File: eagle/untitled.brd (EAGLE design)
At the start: 50 x 50 mm, 38 parts, among them J1 JTAG, U1 MMA3202KEG

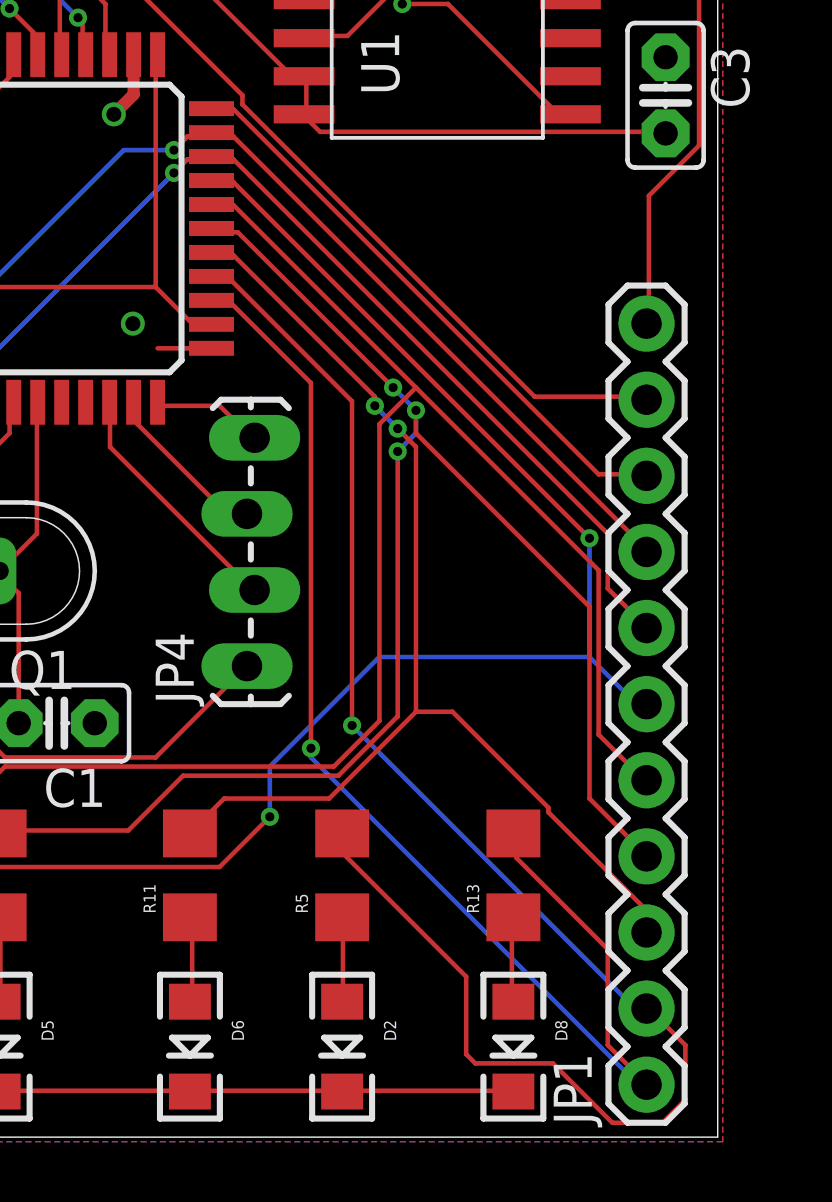
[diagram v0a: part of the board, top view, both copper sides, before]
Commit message: Add pin labels.
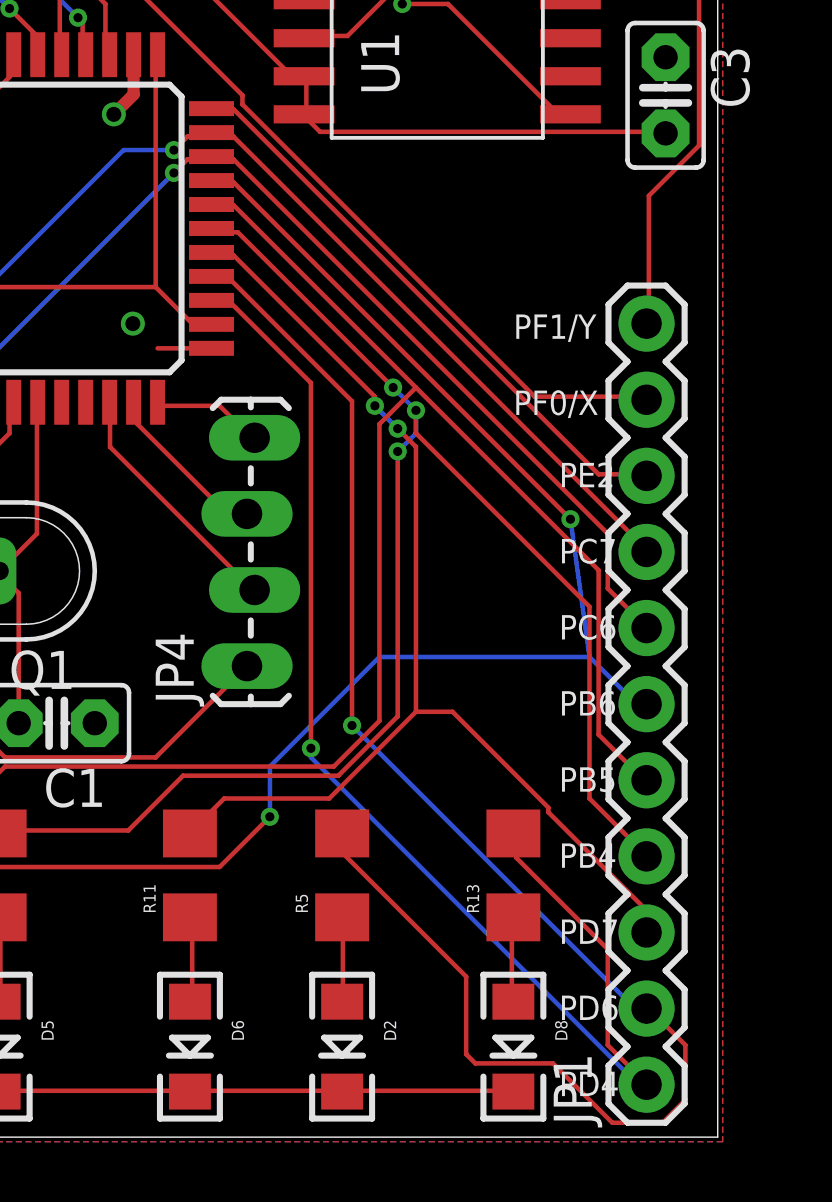
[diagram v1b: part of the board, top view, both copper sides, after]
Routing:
- net PD4: track 42.9 -> 44.1 mm
- net PD6: track 52.3 -> 53.4 mm
- net PB5: track 57.3 -> 57.9 mm
- net PE2: track 19.6 -> 20.2 mm
- net PD7: track 39.0 -> 39.7 mm
- net Y: track 37.3 -> 37.9 mm
- net PC6: track 56.3 -> 56.9 mm
- net PB4: track 52.8 -> 53.4 mm
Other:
- board text added: "PB4"
- board text added: "PB5"
- board text added: "PB6"
- board text added: "PC6"
- board text added: "PC7"
- board text added: "PD4"
- board text added: "PD6"
- board text added: "PD7"
- board text added: "PE2"
- board text added: "PF0/X"
- board text added: "PF1/Y"
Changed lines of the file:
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@@
 <wire x1="0" y1="80" x2="0" y2="30" width="0" layer="20"/>
 <text x="41.91" y="77.47" size="1.778" layer="21">UP -&gt;</text>
+<text x="44.704" y="31.369" size="0.8128" layer="21" font="vector">PD4</text>
+<text x="44.704" y="33.909" size="0.8128" layer="21" font="vector">PD6</text>
+<text x="44.704" y="36.449" size="0.8128" layer="21" font="vector">PD7</text>
+<text x="44.704" y="38.989" size="0.8128" layer="21" font="vector">PB4</text>
+<text x="44.704" y="41.529" size="0.8128" layer="21" font="vector">PB5</text>
+<text x="44.704" y="44.069" size="0.8128" layer="21" font="vector">PB6</text>
+<text x="44.704" y="46.609" size="0.8128" layer="21" font="vector">PC6</text>
+<text x="44.704" y="49.149" size="0.8128" layer="21" font="vector">PC7</text>
+<text x="44.704" y="51.689" size="0.8128" layer="21" font="vector">PE2</text>
+<text x="43.18" y="54.102" size="0.8128" layer="21" font="vector">PF0/X</text>
+<text x="43.18" y="56.642" size="0.8128" layer="21" font="vector">PF1/Y</text>
 </plain>
 <attributes>
@@
 <wire x1="34.1376" y1="64.77" x2="34.1376" y2="64.4652" width="0.1524" layer="1"/>
 <wire x1="28.194" y1="70.7136" x2="34.1376" y2="64.77" width="0.1524" layer="1"/>
-<wire x1="47.5488" y1="54.7116" x2="47.625" y2="54.61" width="0.1524" layer="1"/>
+<wire x1="47.5488" y1="54.7116" x2="48.26" y2="54.61" width="0.1524" layer="1"/>
 <wire x1="28.194" y1="70.7136" x2="28.575" y2="71.12" width="0.1524" layer="1"/>
 </signal>
@@
 <wire x1="49.3776" y1="75.1332" x2="49.3776" y2="63.0936" width="0.1524" layer="1"/>
 <wire x1="48.3108" y1="76.2" x2="49.3776" y2="75.1332" width="0.1524" layer="1"/>
-<wire x1="47.7012" y1="57.15" x2="47.625" y2="57.15" width="0.1524" layer="1"/>
+<wire x1="47.7012" y1="57.15" x2="48.26" y2="57.15" width="0.1524" layer="1"/>
 <wire x1="48.3108" y1="76.2" x2="48.26" y2="76.2" width="0.1524" layer="1"/>
 <wire x1="26.3652" y1="65.3796" x2="26.3652" y2="65.9892" width="0.1524" layer="1"/>
@@
 <wire x1="41.148" y1="44.196" x2="44.3484" y2="40.9956" width="0.1524" layer="1"/>
 <wire x1="39.9288" y1="44.196" x2="41.148" y2="44.196" width="0.1524" layer="1"/>
-<wire x1="47.5488" y1="36.8808" x2="47.625" y2="36.83" width="0.1524" layer="1"/>
+<wire x1="47.5488" y1="36.8808" x2="48.26" y2="36.83" width="0.1524" layer="1"/>
 <via x="38.5572" y="54.4068" extent="1-16" drill="0.3048"/>
 <via x="39.3192" y="53.6448" extent="1-16" drill="0.3048"/>
@@
 <wire x1="47.5488" y1="31.8516" x2="47.244" y2="31.8516" width="0.1524" layer="16"/>
 <wire x1="33.2232" y1="57.912" x2="33.105" y2="57.925" width="0.1524" layer="1"/>
-<wire x1="47.5488" y1="31.8516" x2="47.625" y2="31.75" width="0.1524" layer="16"/>
+<wire x1="47.5488" y1="31.8516" x2="48.26" y2="31.75" width="0.1524" layer="16"/>
 <via x="36.4236" y="42.9768" extent="1-16" drill="0.3048"/>
 <wire x1="43.2816" y1="39.3192" x2="43.2816" y2="40.0812" width="0.1524" layer="1"/>
@@
 <wire x1="47.5488" y1="31.8516" x2="46.3296" y2="33.0708" width="0.1524" layer="1"/>
 <wire x1="43.2816" y1="40.0812" x2="43.18" y2="40.135" width="0.1524" layer="1"/>
-<wire x1="47.5488" y1="31.8516" x2="47.625" y2="31.75" width="0.1524" layer="1"/>
+<wire x1="47.5488" y1="31.8516" x2="48.26" y2="31.75" width="0.1524" layer="1"/>
 </signal>
 <signal name="PD6">
@@
 <wire x1="37.7952" y1="43.7388" x2="37.7952" y2="54.5592" width="0.1524" layer="1"/>
 <wire x1="47.244" y1="34.29" x2="37.7952" y2="43.7388" width="0.1524" layer="16"/>
-<wire x1="47.625" y1="34.29" x2="47.244" y2="34.29" width="0.1524" layer="16"/>
+<wire x1="48.26" y1="34.29" x2="47.244" y2="34.29" width="0.1524" layer="16"/>
 <wire x1="33.2232" y1="58.674" x2="33.105" y2="58.725" width="0.1524" layer="1"/>
 <wire x1="37.4904" y1="39.4716" x2="37.4904" y2="40.0812" width="0.1524" layer="1"/>
@@
 <wire x1="47.7012" y1="34.29" x2="48.9204" y2="33.0708" width="0.1524" layer="1"/>
 <wire x1="37.4904" y1="40.0812" x2="37.465" y2="40.135" width="0.1524" layer="1"/>
-<wire x1="47.7012" y1="34.29" x2="47.625" y2="34.29" width="0.1524" layer="1"/>
+<wire x1="47.7012" y1="34.29" x2="48.26" y2="34.29" width="0.1524" layer="1"/>
 <via x="37.7952" y="43.7388" extent="1-16" drill="0.3048"/>
 </signal>
@@
 <contactref element="R6" pad="2"/>
 <wire x1="33.8328" y1="61.8744" x2="33.2232" y2="61.8744" width="0.1524" layer="1"/>
-<wire x1="45.72" y1="49.9872" x2="33.8328" y2="61.8744" width="0.1524" layer="1"/>
-<wire x1="45.72" y1="46.0248" x2="45.72" y2="49.9872" width="0.1524" layer="16"/>
+<wire x1="45.085" y1="50.6222" x2="33.8328" y2="61.8744" width="0.1524" layer="1"/>
+<wire x1="45.72" y1="46.0248" x2="45.085" y2="50.6222" width="0.1524" layer="16"/>
 <wire x1="47.244" y1="44.5008" x2="45.72" y2="46.0248" width="0.1524" layer="16"/>
 <wire x1="47.5488" y1="44.5008" x2="47.244" y2="44.5008" width="0.1524" layer="16"/>
 <wire x1="33.2232" y1="61.8744" x2="33.105" y2="61.925" width="0.1524" layer="1"/>
-<wire x1="47.5488" y1="44.5008" x2="47.625" y2="44.45" width="0.1524" layer="16"/>
+<wire x1="47.5488" y1="44.5008" x2="48.26" y2="44.45" width="0.1524" layer="16"/>
 <wire x1="14.6304" y1="42.2148" x2="14.6304" y2="40.2336" width="0.1524" layer="1"/>
 <wire x1="17.3736" y1="44.958" x2="14.6304" y2="42.2148" width="0.1524" layer="1"/>
@@
 <wire x1="45.72" y1="46.0248" x2="38.7096" y2="46.0248" width="0.1524" layer="16"/>
 <wire x1="14.6304" y1="40.2336" x2="14.605" y2="40.135" width="0.1524" layer="1"/>
-<via x="45.72" y="49.9872" extent="1-16" drill="0.3048"/>
+<via x="45.085" y="50.6222" extent="1-16" drill="0.3048"/>
 <via x="35.052" y="40.6908" extent="1-16" drill="0.3048"/>
 </signal>
@@
 <wire x1="47.5488" y1="47.0916" x2="46.3296" y2="48.3108" width="0.1524" layer="1"/>
 <wire x1="33.2232" y1="62.6364" x2="33.105" y2="62.725" width="0.1524" layer="1"/>
-<wire x1="47.5488" y1="47.0916" x2="47.625" y2="46.99" width="0.1524" layer="1"/>
+<wire x1="47.5488" y1="47.0916" x2="48.26" y2="46.99" width="0.1524" layer="1"/>
 <wire x1="9.906" y1="40.2336" x2="8.382" y2="40.2336" width="0.1524" layer="1"/>
 <wire x1="20.2692" y1="50.5968" x2="9.906" y2="40.2336" width="0.1524" layer="1"/>
@@
 <wire x1="47.7012" y1="49.53" x2="33.8328" y2="63.3984" width="0.1524" layer="1"/>
 <wire x1="33.2232" y1="63.3984" x2="33.105" y2="63.525" width="0.1524" layer="1"/>
-<wire x1="47.7012" y1="49.53" x2="47.625" y2="49.53" width="0.1524" layer="1"/>
+<wire x1="47.7012" y1="49.53" x2="48.26" y2="49.53" width="0.1524" layer="1"/>
 <wire x1="6.2484" y1="40.2336" x2="1.9812" y2="40.2336" width="0.1524" layer="1"/>
 <wire x1="17.526" y1="51.5112" x2="6.2484" y2="40.2336" width="0.1524" layer="1"/>
@@
 <wire x1="47.5488" y1="39.4716" x2="45.72" y2="41.3004" width="0.1524" layer="1"/>
 <wire x1="33.2232" y1="60.198" x2="33.105" y2="60.325" width="0.1524" layer="1"/>
-<wire x1="47.5488" y1="39.4716" x2="47.625" y2="39.37" width="0.1524" layer="1"/>
+<wire x1="47.5488" y1="39.4716" x2="48.26" y2="39.37" width="0.1524" layer="1"/>
 <wire x1="30.3276" y1="40.2336" x2="26.0604" y2="40.2336" width="0.1524" layer="1"/>
 <wire x1="32.1564" y1="42.0624" x2="30.3276" y2="40.2336" width="0.1524" layer="1"/>
@@
 <wire x1="47.5488" y1="41.91" x2="46.0248" y2="43.434" width="0.1524" layer="1"/>
 <wire x1="33.2232" y1="61.1124" x2="33.105" y2="61.125" width="0.1524" layer="1"/>
-<wire x1="47.5488" y1="41.91" x2="47.625" y2="41.91" width="0.1524" layer="1"/>
+<wire x1="47.5488" y1="41.91" x2="48.26" y2="41.91" width="0.1524" layer="1"/>
 <wire x1="24.0792" y1="40.2336" x2="20.4216" y2="40.2336" width="0.1524" layer="1"/>
 <wire x1="26.2128" y1="42.3672" x2="24.0792" y2="40.2336" width="0.1524" layer="1"/>
@@
 <wire x1="47.5488" y1="52.1208" x2="46.0248" y2="52.1208" width="0.1524" layer="1"/>
 <wire x1="33.2232" y1="64.3128" x2="33.105" y2="64.325" width="0.1524" layer="1"/>
-<wire x1="47.5488" y1="52.1208" x2="47.625" y2="52.07" width="0.1524" layer="1"/>
+<wire x1="47.5488" y1="52.1208" x2="48.26" y2="52.07" width="0.1524" layer="1"/>
 </signal>
 <signal name="N$2">

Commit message: Smash and rework some labels.
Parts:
- moved JP1 0.63 mm to (48.3, 31.8)
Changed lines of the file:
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@@
 </element>
 <element name="R3" library="SparkFun-Passives" package="1206" value="10k" x="19.685" y="52.705"/>
-<element name="Q1" library="special" package="QS" value="" x="23.495" y="48.895" rot="R180"/>
-<element name="C1" library="capacitor-wima" package="C2.5-2" value="" x="27.94" y="43.815" rot="R180"/>
+<element name="Q1" library="special" package="QS" value="" x="23.495" y="48.895" smashed="yes" rot="R180">
+<attribute name="VALUE" x="28.575" y="52.832" size="1.27" layer="27" ratio="10" rot="R180"/>
+<attribute name="NAME" x="31.75" y="50.673" size="1.27" layer="25" ratio="10" rot="R180"/>
+</element>
+<element name="C1" library="capacitor-wima" package="C2.5-2" value="" x="27.94" y="43.815" smashed="yes" rot="R180">
+<attribute name="NAME" x="29.591" y="46.736" size="1.27" layer="25" ratio="10" rot="R180"/>
+<attribute name="VALUE" x="29.591" y="46.609" size="1.27" layer="27" ratio="10" rot="R180"/>
+</element>
 <element name="C2" library="capacitor-wima" package="C2.5-2" value="" x="19.05" y="43.815"/>
 <element name="U1" library="gipi" package="SOIC20" value="MMA3202KEG" x="40.64" y="69.85"/>
-<element name="G1" library="battery" package="10MM_SM_COIN_CELL_CLIP" value="BAT" x="5.715" y="50.165" rot="R90"/>
-<element name="C3" library="capacitor-wima" package="C2.5-2" value="" x="48.26" y="64.77" rot="R270"/>
+<element name="G1" library="battery" package="10MM_SM_COIN_CELL_CLIP" value="BAT" x="5.715" y="50.165" smashed="yes" rot="R90">
+<attribute name="NAME" x="2.99248125" y="56.20125" size="1.27" layer="25" font="vector" rot="R90"/>
+<attribute name="VALUE" x="12.15435" y="45.68245" size="1.27" layer="27" font="vector" rot="R90"/>
+</element>
+<element name="C3" library="capacitor-wima" package="C2.5-2" value="" x="48.26" y="64.77" smashed="yes" rot="R270">
+<attribute name="NAME" x="47.244" y="67.691" size="1.27" layer="25" ratio="10"/>
+<attribute name="VALUE" x="45.466" y="66.421" size="1.27" layer="27" ratio="10" rot="R270"/>
+</element>
 <element name="SJ1" library="SparkFun-Retired" package="SJ_3_PASTE2&amp;3" value="" x="29.21" y="77.47" rot="R180"/>
 <element name="R9" library="SparkFun-Passives" package="1206" value="10k" x="33.02" y="76.2" rot="R270"/>
 <element name="R10" library="SparkFun-Passives" package="1206" value="10k" x="24.13" y="71.12" rot="R180"/>
 <element name="C4" library="capacitor-wima" package="C2.5-2" value="" x="29.845" y="71.12" rot="R180"/>
-<element name="C5" library="capacitor-wima" package="C2.5-2" value="" x="48.26" y="74.93" rot="R90"/>
+<element name="C5" library="capacitor-wima" package="C2.5-2" value="" x="48.26" y="74.93" smashed="yes" rot="R90">
+<attribute name="NAME" x="49.276" y="72.136" size="1.27" layer="25" ratio="10" rot="R180"/>
+<attribute name="VALUE" x="51.054" y="73.279" size="1.27" layer="27" ratio="10" rot="R90"/>
+</element>
 <element name="C6" library="capacitor-wima" package="C2.5-2" value="1uf" x="14.605" y="64.77" rot="R180"/>
 <element name="JP4" library="SparkFun-Connectors" package="1X04_LOCK_LONGPADS" value="SERIAL" x="34.29" y="45.72" rot="R90"/>
 <element name="JP5" library="SparkFun-Connectors" package="2X3" value="PRG" x="13.335" y="60.325" rot="R270"/>
-<element name="JP1" library="SparkFun-Connectors" package="1X11" value="M11PTH" x="47.625" y="31.75" rot="R90"/>
+<element name="JP1" library="SparkFun-Connectors" package="1X11" value="M11PTH" x="48.26" y="31.75" smashed="yes" rot="R90">
+<attribute name="NAME" x="48.9712" y="26.5938" size="1.27" layer="25" ratio="10" rot="R90"/>
+<attribute name="VALUE" x="51.435" y="30.48" size="1.27" layer="27" rot="R90"/>
+</element>
 <element name="R4" library="SparkFun-Passives" package="1206" value="" x="1.905" y="38.735" rot="R90"/>
 <element name="D1" library="SparkFun-LED" package="LED-1206" value="" x="1.905" y="33.02" rot="R270"/>
@@
 <element name="R12" library="SparkFun-Passives" package="1206" value="" x="8.255" y="38.735" rot="R90"/>
 <element name="R13" library="SparkFun-Passives" package="1206" value="" x="43.18" y="38.735" rot="R90"/>
-<element name="J1" library="con-headers-jp" package="DIL-2MM-2X05" value="JTAG" x="22.225" y="76.835"/>
+<element name="J1" library="con-headers-jp" package="DIL-2MM-2X05" value="JTAG" x="22.225" y="76.835" smashed="yes">
+<attribute name="NAME" x="16.225" y="76.105" size="1.016" layer="25" ratio="18" rot="R90"/>
+<attribute name="VALUE" x="18.51" y="73.675" size="0.8128" layer="27" ratio="10" rot="R180"/>
+</element>
 </elements>
 <signals>

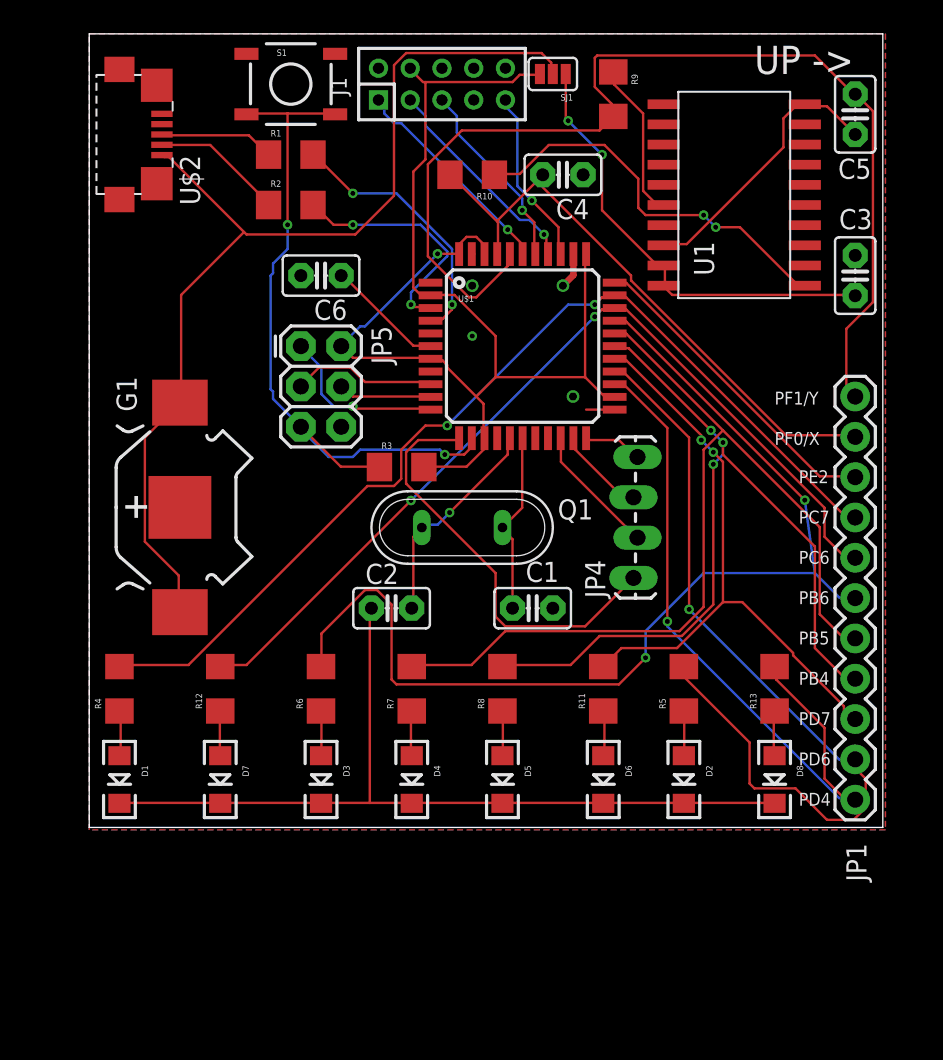
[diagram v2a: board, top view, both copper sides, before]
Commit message: Replace usb micro connector with mini type.
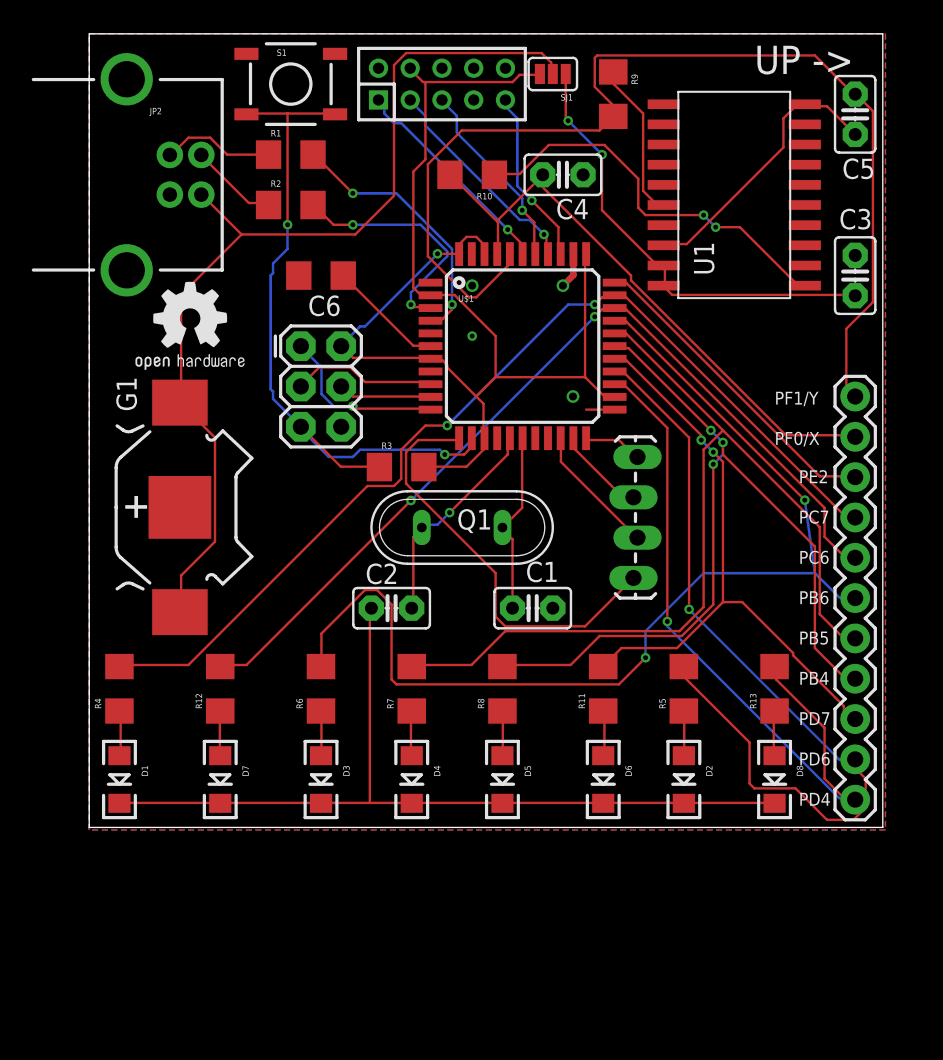
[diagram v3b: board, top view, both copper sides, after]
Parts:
- removed U$2: USB, con-hirose:ZX62R-B-5P
- added GOLD_ORB_SM1: OSHWLOGO_GOLD_ORB_SM, bfl:OSHW2
- added JP2: USB-B, SparkFun-Connectors:USB-B-PTH
- C6: device capacitor-wima:C2.5-2 -> eagle-ltspice:C1206
- JP5: value PRG -> ICSP
- Q1: value (none) -> 16MHz
- S1: value TAC_SWITCHSMD -> RESET
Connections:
- removed net N$18: G1.+@1, G1.+@2, SJ1.2, U$2.1
- new net N$28: G1.+@1, G1.+@2, JP2.VBUS, SJ1.2
- net GND-ISO: now also JP2.GND; no longer U$2.4, U$2.5
- net N$3: now also JP2.D-; no longer U$2.2
- net N$4: now also JP2.D+; no longer U$2.3
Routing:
- net N$18: track 64.6 -> 0.00 mm
- net N$28: track 0.00 -> 60.9 mm
- net N$3: track 8.34 -> 5.61 mm
